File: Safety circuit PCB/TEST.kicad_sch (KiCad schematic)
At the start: 31 parts, among them J1 430450801, J2 430450801, J3 DT13-12PA-B016, Q1 2N7002K, Q2 2N7002K, Q3 2N7002K, Q4 2N7002K, Q5 2N7002K, Q6 2N7002K, Q7 2N7002K

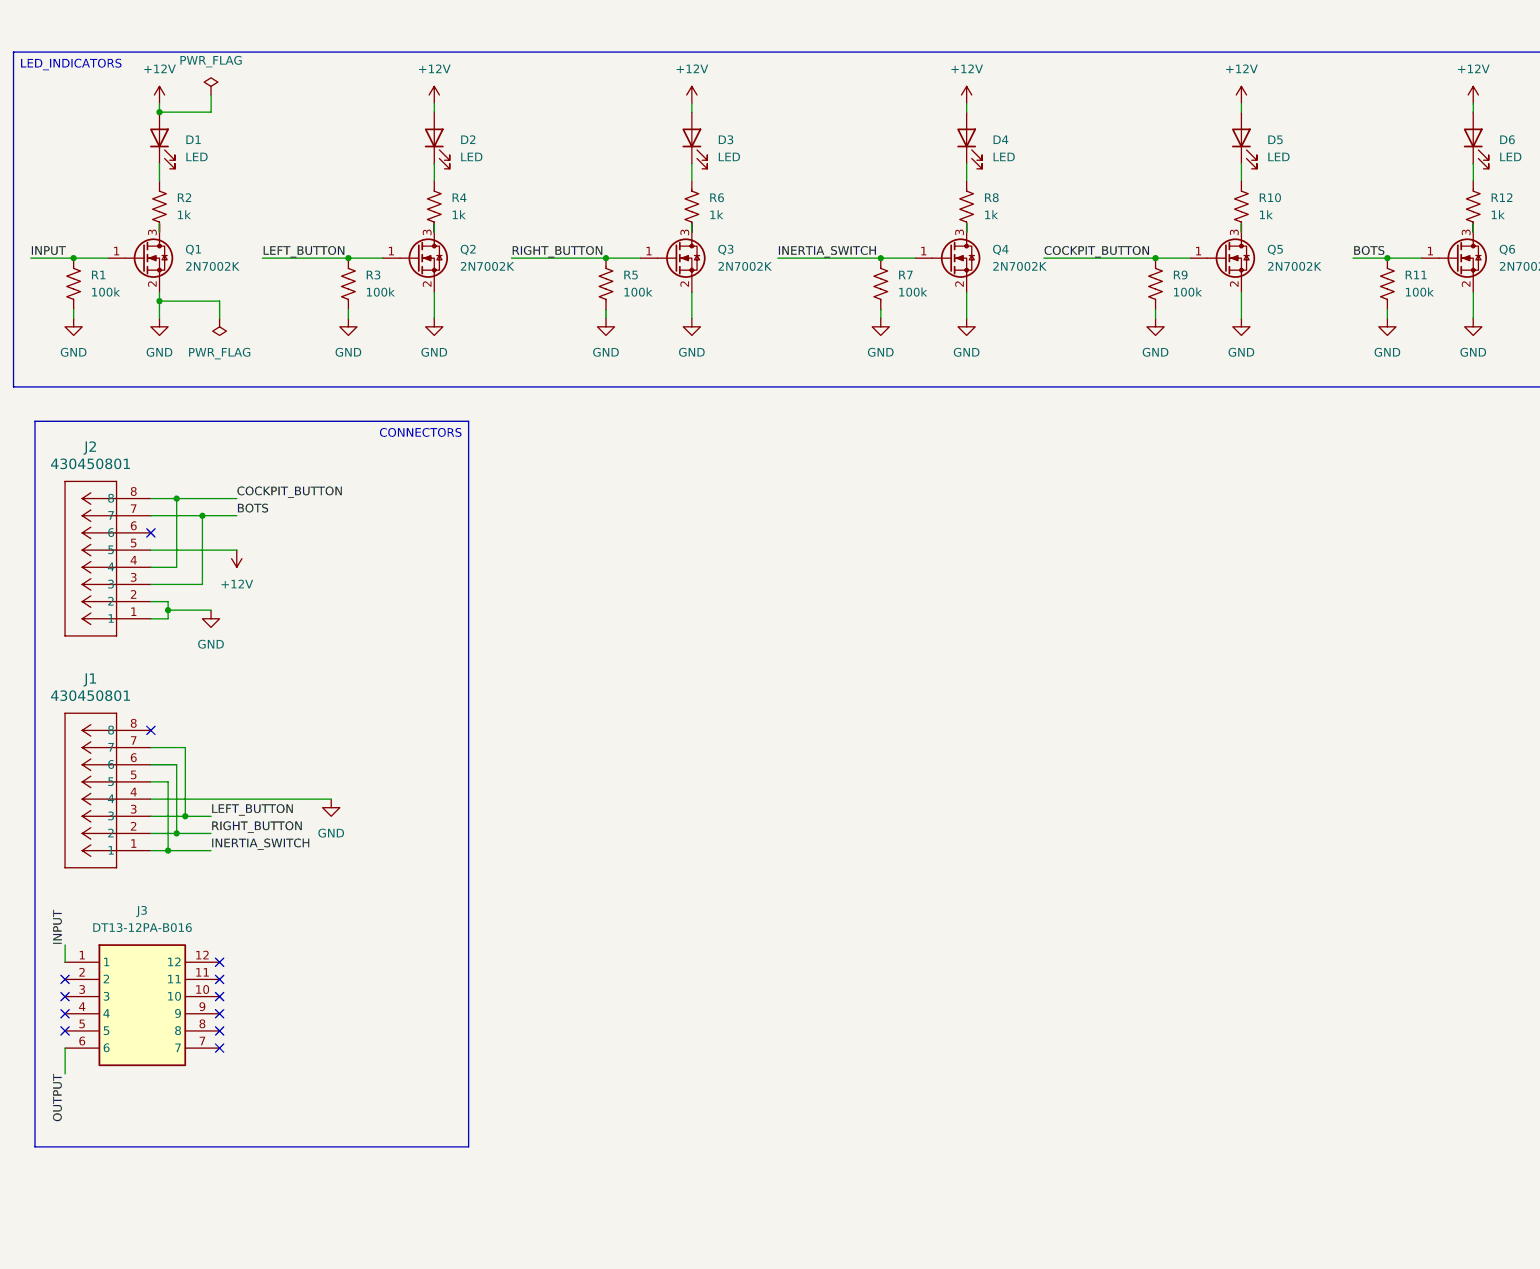
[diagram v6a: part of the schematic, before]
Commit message: Connector refactor
Add nanofit for input and output, remove two 8-pin connectors. Still need to stitch board and regenerate gerbers.
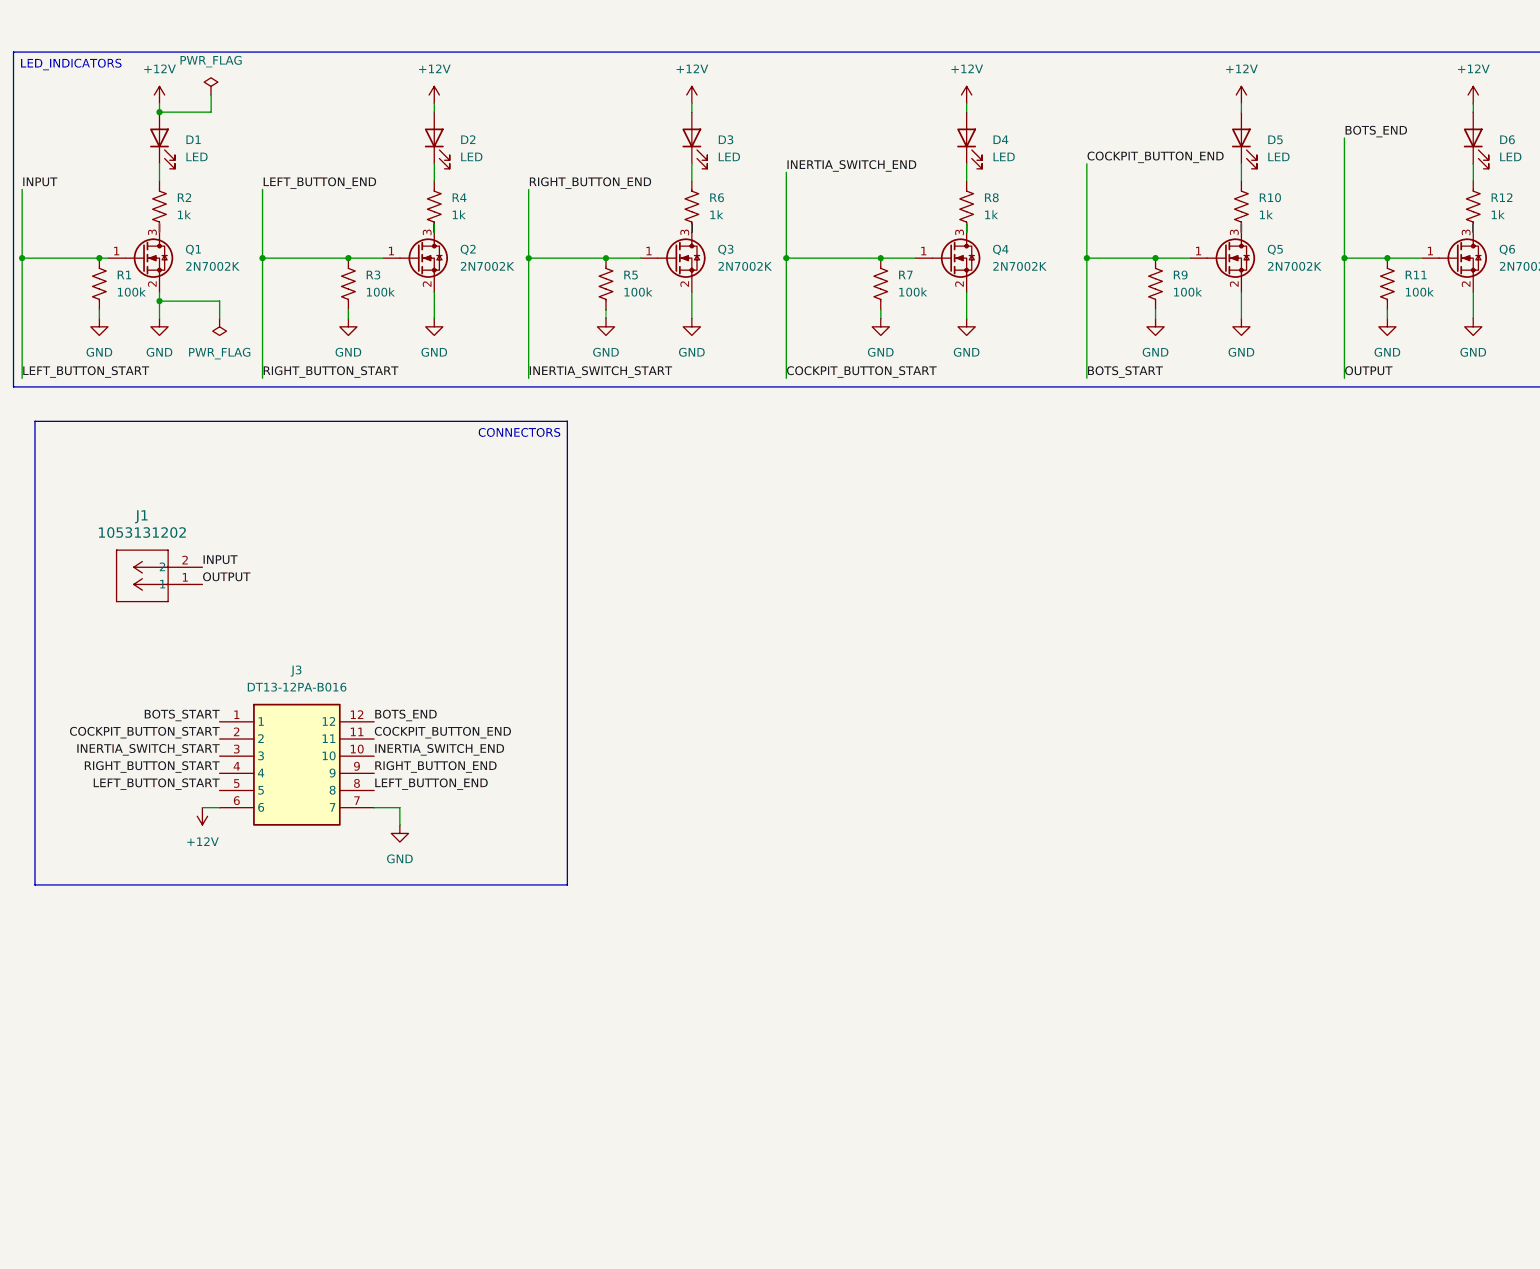
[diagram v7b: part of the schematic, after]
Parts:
- removed J1, J2: 430450801, SC:CONN_SD-43045-001_08_MOL, symbol SC:430450801
- added J1: 1053131202, CONN_SD-105313-100_02_MOL, symbol Molex-1053131202:1053131202
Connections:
- net BOTS is gone; now on net BOTS_END: Q6.1 (G), R11.1
- net COCKPIT_BUTTON is gone; now on net BOTS_START: Q5.1 (G), R9.1
- net INERTIA_SWITCH is gone; now on net COCKPIT_BUTTON_START: Q4.1 (G), R7.1
- net LEFT_BUTTON is gone; now on net LEFT_BUTTON_END: Q2.1 (G), R3.1
- net RIGHT_BUTTON is gone; now on net INERTIA_SWITCH_START: Q3.1 (G), R5.1
- net +12V: now also J3.6
- net GND: now also J3.7
- net INPUT: now also J3.5, J1.2; no longer J3.1
- net COCKPIT_BUTTON_START: now reaches J3.10
- net COCKPIT_BUTTON_START: now also J3.2
- net BOTS_START: now reaches J3.11
- net BOTS_START: now also J3.1
- net BOTS_END: now reaches J3.12
- net BOTS_END: now also Q7.1 (G), R13.1, J1.1
- net INERTIA_SWITCH_START: now reaches J3.3
- net INERTIA_SWITCH_START: now also J3.9
- net LEFT_BUTTON_END: now reaches J3.4
- net LEFT_BUTTON_END: now also J3.8
- removed net OUTPUT: J3.6, Q7.1 (G), R13.1
- no-connect marks 12 -> 0
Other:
- moved on the sheet: J3, R1

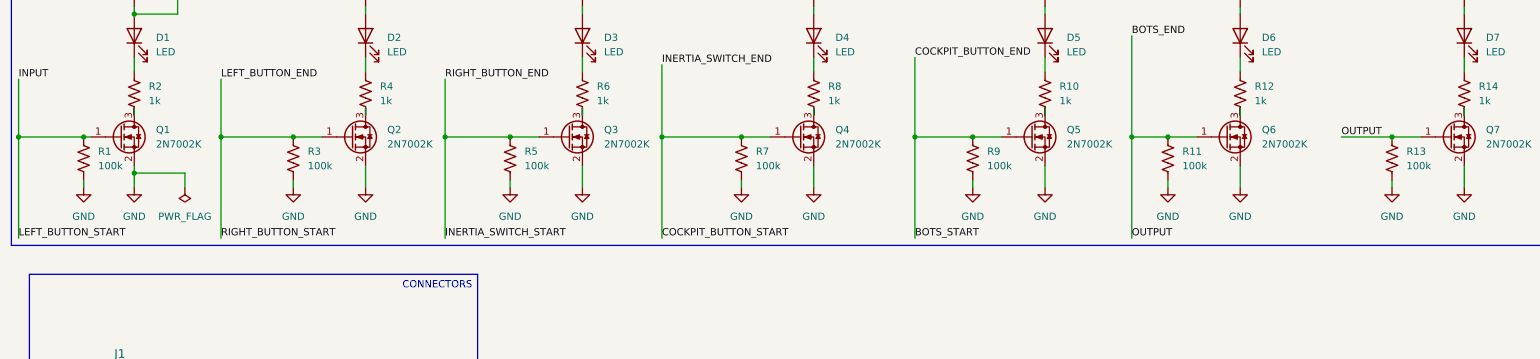
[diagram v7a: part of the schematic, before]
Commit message: Remove pull down resistors at MOSFET gates and increase sizes of traces
Also some more nice via tracing.
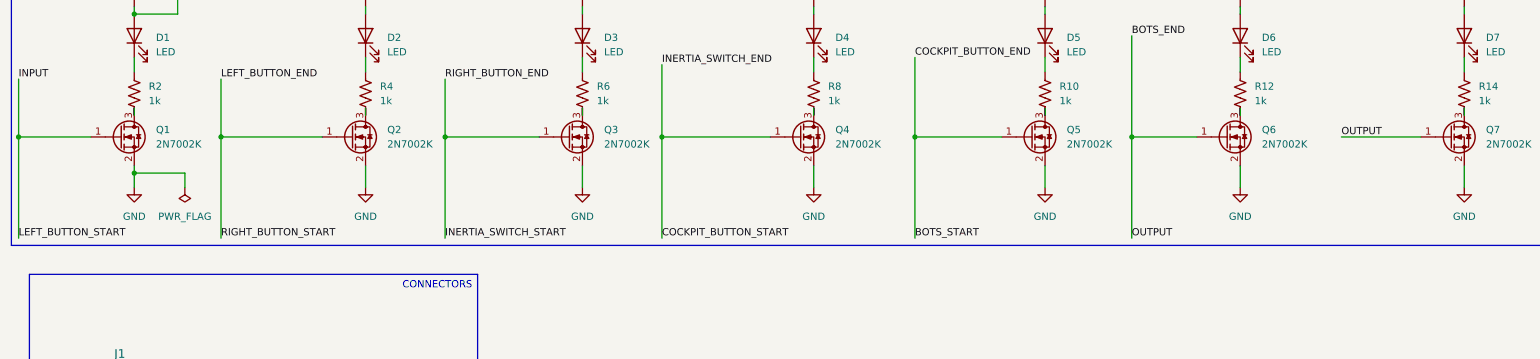
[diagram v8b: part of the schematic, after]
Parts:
- removed R1, R11, R13, R3, R5, R7, R9: 100k, SC:CRCW0805, symbol Device:R_US
